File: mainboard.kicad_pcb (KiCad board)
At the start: 4 copper layers, 44.4 x 35.8 mm, 73 parts, among them J1 Conn_01x06, J2 USB_B_Micro, J3 xf2m-2415-1a, J4 XF2M-1015-1A, J5 Conn_01x02, J6 U.FL-R-SMT-1, J7 Conn_02x02_Top_Bottom, Q1 RADFET, SW1 KMR231NG LFS, U1 BMX160, U11 AP2112K-3.3, U2 MAX708RESA-T, U3 ATSAMD51J20A-M, U4 DRV8830DRC, U5 MR25H40, U6 DRV8830DRC, U7 ADS124S06IRHBR, U8 DRV8830DRC, U9 RFM98PW-symbols

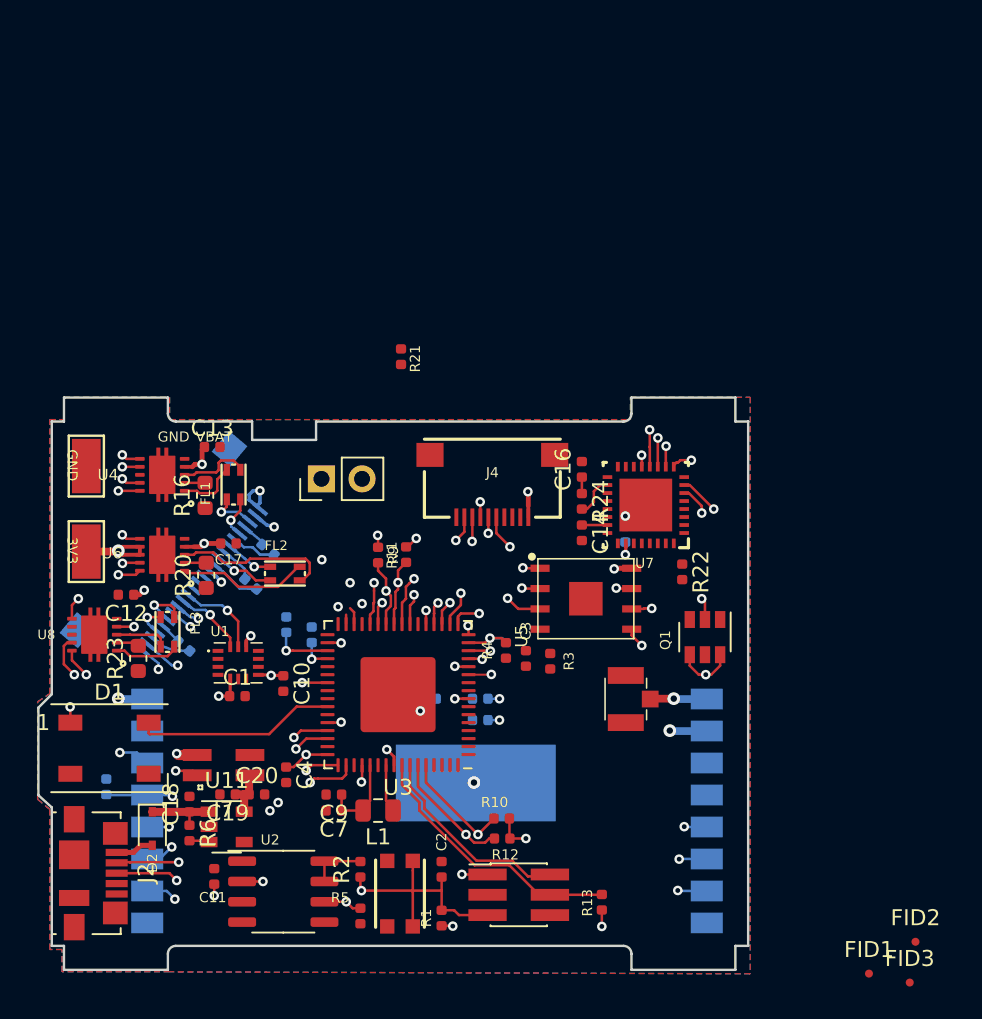
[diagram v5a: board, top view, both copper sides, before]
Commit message: removed dosimeter & roughed in new RBF header
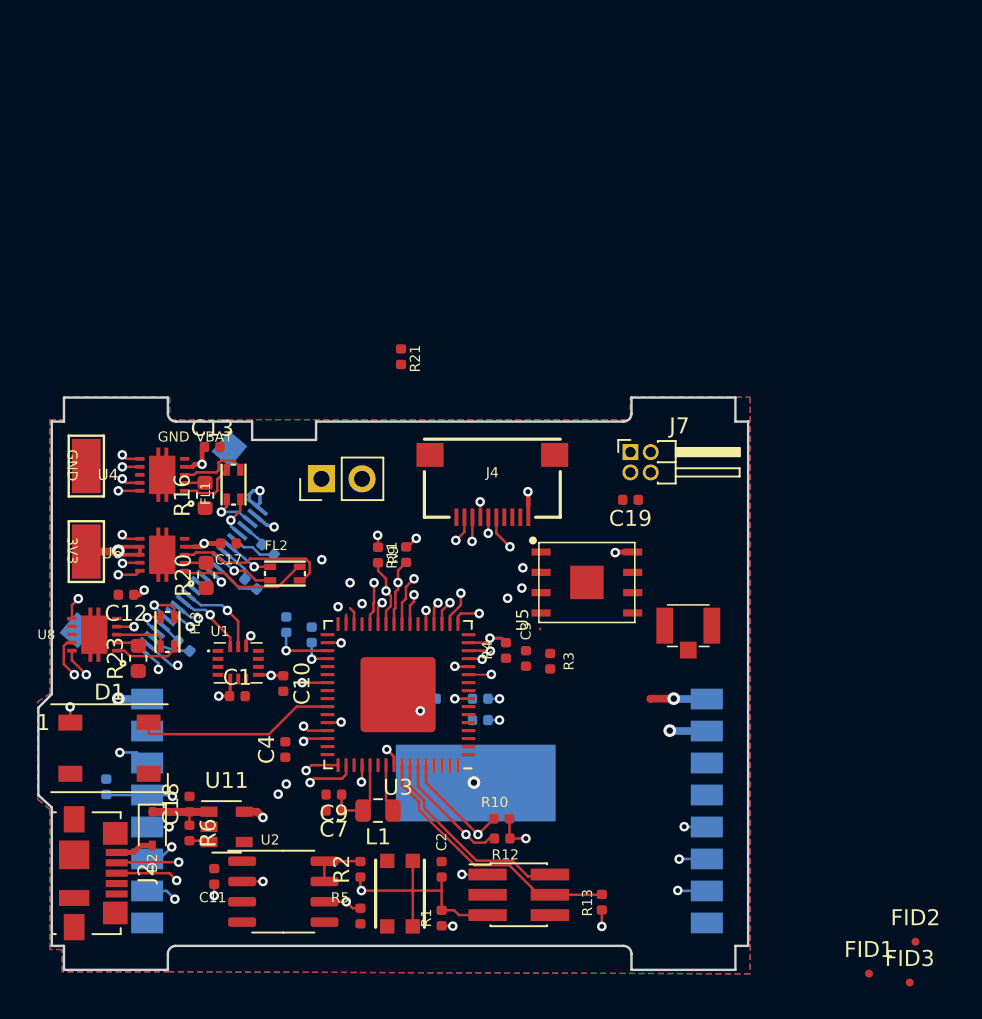
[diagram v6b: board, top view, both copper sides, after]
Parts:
- removed C14, C20: 1uF, Capacitor_SMD:C_0402_1005Metric
- removed C15, C16: 0.1uF, Capacitor_SMD:C_0402_1005Metric
- removed Q1: RADFET, Package_TO_SOT_SMD:SOT-23-6
- removed R22, R24: 10K, Resistor_SMD:R_0402_1005Metric
- removed U7: ADS124S06IRHBR, custom-footprints:ADS124208_withpad
- J7: footprint Connector_PinSocket_1.27mm:PinSocket_2x02_P1.27mm_Vertical_SMD -> Connector_PinHeader_1.27mm:PinHeader_2x02_P1.27mm_Horizontal
- moved J7 32.1 mm to (113.5, 76.3), turned to 0 degrees
- moved C19 31.2 mm to (113.5, 79.3)
- moved J6 6.03 mm to (117.2, 87.2), turned to 0 degrees
- moved C4 1.58 mm to (91.9, 94.9), turned to 90 degrees
- moved U5 1.02 mm to (110.8, 84.5)
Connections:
- J7 pad 1: +3V3 -> GND
- J7 pad 2: Net-(C19-Pad1) -> BATT_P
- J7 pad 3: BATT_P -> +3V3
- J7 pad 4: GND -> Net-(C19-Pad1)
- U3 pad 11: ADC_CS -> Net-(U3-Pad11)
- U3 pad 16: ADC_DRDY -> Net-(U3-Pad16)
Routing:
- net Net-(C19-Pad1): track 3.16 -> 40.6 mm, vias 0 -> 1
- net ADC_DRDY: track 22.0 -> 0.00 mm, vias 2 -> 0
- net MISO: track 58.2 -> 41.3 mm, vias 4 -> 3
- net SCK: track 54.3 -> 38.0 mm, vias 4 -> 3
- net MOSI: track 54.2 -> 38.9 mm, vias 4 -> 3
- net BATT_P: track 61.8 -> 51.4 mm, vias 8 -> 7
- net Net-(Q1-Pad4): track 6.92 -> 0.00 mm, vias 2 -> 0
- net +3V3: track 31.9 -> 25.8 mm, vias 22 -> 19
- net FLASH_MOSI: track 14.5 -> 10.6 mm, vias 2 -> 1
- net Net-(Q1-Pad2): track 3.26 -> 0.00 mm, vias 2 -> 0
- net ADC_CS: track 2.75 -> 0.00 mm, vias 2 -> 0
- net Net-(R24-Pad2): track 2.62 -> 0.00 mm
- net FLASH_SCK: track 19.1 -> 16.7 mm, vias 2 -> 1
- net FLASH_IO2: track 8.01 -> 5.70 mm
- net FLASH_IO3: track 14.4 -> 12.6 mm, vias 2 -> 1
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
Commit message: roughed-in SD card
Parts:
- added J8: Micro_SD_Card, Connector_Card:microSD_HC_Molex_104031-0811, F.Cu at (113.5, 96.6)
- moved R13 12.7 mm to (99.8, 100.3), turned to 180 degrees
- moved R3 7.16 mm to (103.8, 84.0)
- moved C3 4.70 mm to (104.8, 85.1)
- moved J1 2.39 mm to (104.3, 103.3), turned to 90 degrees
- moved C18 2.03 mm to (85.8, 96.3)
- moved U11 1.92 mm to (88.2, 97.9)
- moved R12 1.89 mm to (105.2, 98.6), turned to 90 degrees
- moved R6 1.67 mm to (85.8, 98.5)
- moved R10 1.64 mm to (103.9, 98.7), turned to 90 degrees
- moved J6 1.11 mm to (118.1, 87.8)
- moved C11 1.00 mm to (86.6, 102.6)
- moved R5 1.00 mm to (95.7, 105.0)
- moved U2 1.00 mm to (90.9, 103.5)
- moved C2 1.00 mm to (100.8, 102.1)
- moved R1 1.00 mm to (100.8, 105.2)
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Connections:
- net RF_IO2 renamed Net-(U9-Pad8)
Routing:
- net SWCLK: track 16.9 -> 3.28 mm
- net SWDIO: track 12.7 -> 3.07 mm
- net +3V3: track 25.8 -> 19.8 mm, vias 19 -> 15
- net SCL3: track 56.7 -> 51.2 mm
- net SDA3: track 59.8 -> 55.1 mm
- net ~RESET: track 23.2 -> 20.2 mm
- net Net-(C19-Pad1): track 40.6 -> 39.2 mm, vias 1 -> 0
- net Net-(J6-Pad3): track 3.56 -> 2.58 mm
- net RF_IO0: track 24.0 -> 24.6 mm
- net GND: track 8.87 -> 8.34 mm

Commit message: routed
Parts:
- TP1, TP2: footprint TestPoint:TestPoint_Keystone_5015_Micro-Minature -> TestPoint:TestPoint_Pad_1.0x1.0mm
- moved FID3 59.4 mm to (79.6, 79.8)
- moved FID2 35.9 mm to (111.3, 77.2)
- moved R21 17.4 mm to (91.6, 86.0), turned to 180 degrees
- moved FID1 16.9 mm to (114.5, 99.4)
- moved R12 12.5 mm to (92.7, 97.7), turned to 270 degrees
- moved R10 12.3 mm to (91.6, 98.6), turned to 270 degrees
- moved R3 6.08 mm to (107.8, 88.6), turned to 0 degrees
- moved C3 5.51 mm to (107.8, 89.7), turned to 0 degrees
- moved C11 5.39 mm to (91.6, 100.6), turned to 0 degrees
- moved U5 1.78 mm to (109.2, 85.3)
- moved R4 1.62 mm to (106.2, 90.3)
- moved J1 1.37 mm to (102.9, 103.6), turned to 270 degrees
- moved R2 1.29 mm to (94.5, 101.7)
- moved U2 1.29 mm to (89.7, 103.9)
- moved C2 1.21 mm to (99.6, 102.1)
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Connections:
- J8 pad 2: Net-(J8-Pad2) -> SD_CS
- J8 pad 3: Net-(J8-Pad3) -> MOSI
- J8 pad 4: Net-(J8-Pad4) -> +3V3
- J8 pad 5: Net-(J8-Pad5) -> SCK
- J8 pad 6: Net-(J8-Pad6) -> GND
- J8 pad 7: Net-(J8-Pad7) -> MISO
- J8 pad 9: Net-(J8-Pad9) -> GND
- U3 pad 11: Net-(U3-Pad11) -> SD_CS
- U3 pad 12: RF_CS -> Net-(U3-Pad12)
- U3 pad 27: RF_RST -> M_FAULT
- U3 pad 41: Net-(U3-Pad41) -> RF_RST
- U3 pad 43: Net-(U3-Pad43) -> RF_CS
- U3 pad 62: M_FAULT -> Net-(U3-Pad62)
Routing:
- net BATT_P: track 51.8 -> 91.3 mm, vias 7 -> 8
- net MOSI: track 38.9 -> 74.5 mm, vias 3 -> 4
- net MISO: track 41.3 -> 68.9 mm, vias 3 -> 4
- net SCK: track 38.0 -> 63.9 mm, vias 3 -> 4
- net RF_RST: track 26.2 -> 1.99 mm, vias 2 -> 1
- net SD_CS: track 0.00 -> 19.2 mm, vias 0 -> 2
- net RF_CS: track 26.1 -> 16.0 mm
- net SWDIO: track 3.07 -> 12.0 mm
- net SWCLK: track 3.28 -> 11.9 mm
- net Net-(C19-Pad1): track 39.2 -> 46.8 mm, vias 0 -> 2
- net +3V3: track 19.8 -> 27.1 mm, vias 15 -> 23
- net ~RESET: track 20.2 -> 24.8 mm, vias 2 -> 3
- net /BATTERY: track 3.45 -> 6.18 mm
- net SCL3: track 51.2 -> 53.5 mm
- net SDA3: track 55.1 -> 57.4 mm
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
